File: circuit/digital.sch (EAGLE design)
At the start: 34 parts, among them IC1 MCP1701-5V, IC2 MCP1700-3.3V, X1 MINI-USB-SCHIELD-32005-301

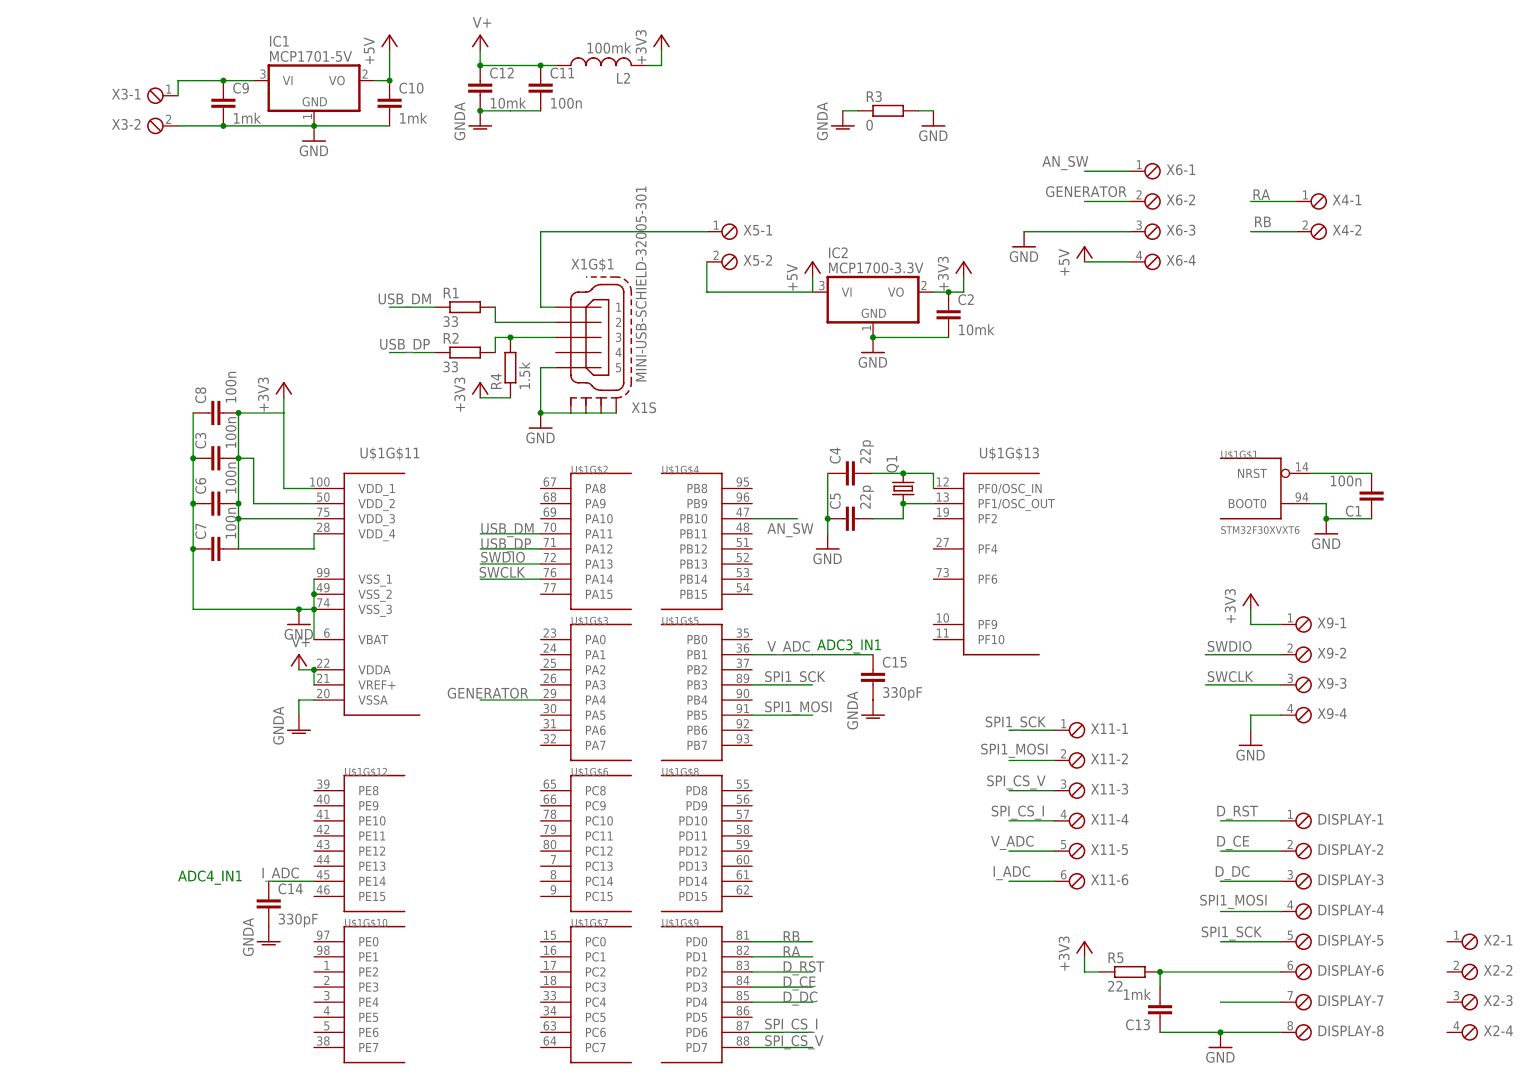
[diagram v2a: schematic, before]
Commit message: - прикрутили коннектор для энкодера
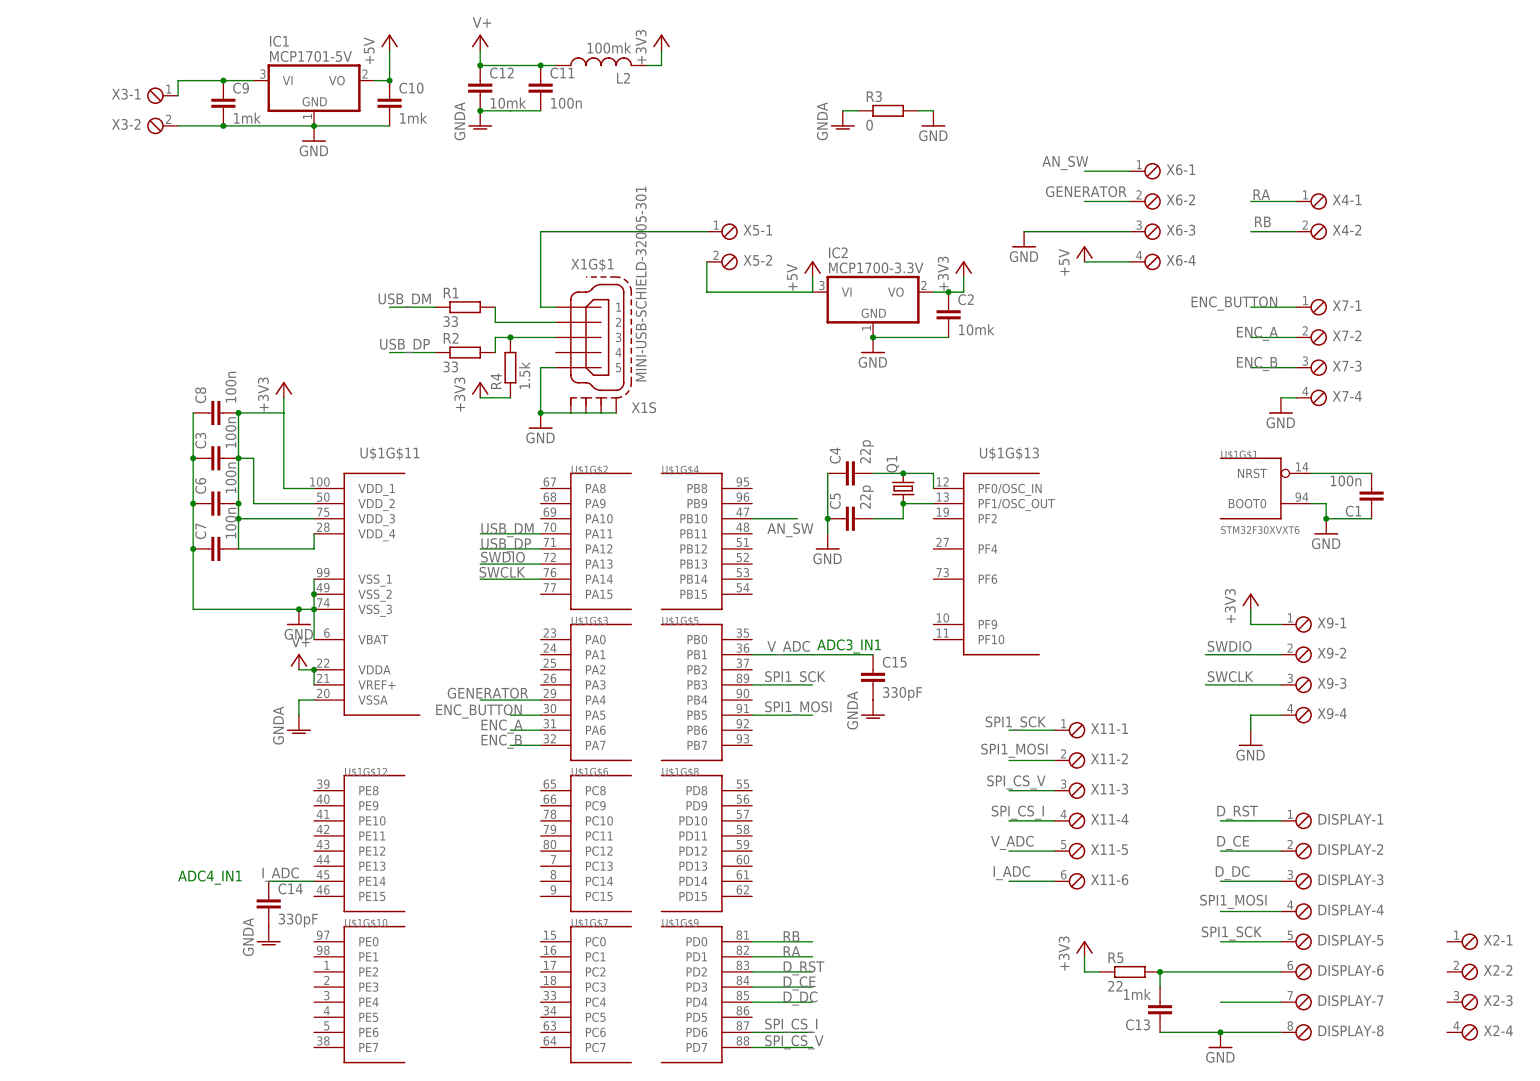
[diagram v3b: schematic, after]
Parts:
- added X7: (no value), con-phoenix-254:MPT4
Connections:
- new net ENC_A: U$1G$3.PA6, X7-2.1
- new net ENC_B: U$1G$3.PA7, X7-3.1
- new net ENC_BUTTON: U$1G$3.PA5, X7-1.1
- net GND: now also X7-4.1
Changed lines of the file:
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@@
 <part name="GND16" library="supply1" deviceset="GND" device=""/>
 <part name="X2" library="con-phoenix-254" deviceset="MPT4" device=""/>
+<part name="X7" library="con-phoenix-254" deviceset="MPT4" device=""/>
+<part name="GND2" library="supply1" deviceset="GND" device=""/>
 </parts>
 <sheets>
@@
 <instance part="X2" gate="-3" x="205.74" y="-58.42"/>
 <instance part="X2" gate="-4" x="205.74" y="-63.5"/>
+<instance part="X7" gate="-1" x="180.34" y="58.42"/>
+<instance part="X7" gate="-2" x="180.34" y="53.34"/>
+<instance part="X7" gate="-3" x="180.34" y="48.26"/>
+<instance part="X7" gate="-4" x="180.34" y="43.18"/>
+<instance part="GND2" gate="1" x="175.26" y="40.64"/>
 </instances>
 <busses>
@@
 <pinref part="GND16" gate="1" pin="GND"/>
 <wire x1="132.08" y1="71.12" x2="142.24" y2="71.12" width="0.1524" layer="91"/>
+</segment>
+<segment>
+<pinref part="X7" gate="-4" pin="1"/>
+<wire x1="177.8" y1="43.18" x2="175.26" y2="43.18" width="0.1524" layer="91"/>
+<pinref part="GND2" gate="1" pin="GND"/>
 </segment>
 </net>
@@
 </segment>
 </net>
+<net name="ENC_BUTTON" class="0">
+<segment>
+<pinref part="X7" gate="-1" pin="1"/>
+<wire x1="177.8" y1="58.42" x2="170.18" y2="58.42" width="0.1524" layer="91"/>
+<label x="160.02" y="58.42" size="1.778" layer="95"/>
+</segment>
+<segment>
+<pinref part="U$1" gate="G$3" pin="PA5"/>
+<wire x1="50.8" y1="-10.16" x2="45.72" y2="-10.16" width="0.1524" layer="91"/>
+<label x="33.02" y="-10.16" size="1.778" layer="95"/>
+</segment>
+</net>
+<net name="ENC_A" class="0">
+<segment>
+<pinref part="X7" gate="-2" pin="1"/>
+<wire x1="177.8" y1="53.34" x2="170.18" y2="53.34" width="0.1524" layer="91"/>
+<label x="167.64" y="53.34" size="1.778" layer="95"/>
+</segment>
+<segment>
+<pinref part="U$1" gate="G$3" pin="PA6"/>
+<wire x1="50.8" y1="-12.7" x2="45.72" y2="-12.7" width="0.1524" layer="91"/>
+<label x="40.64" y="-12.7" size="1.778" layer="95"/>
+</segment>
+</net>
+<net name="ENC_B" class="0">
+<segment>
+<pinref part="X7" gate="-3" pin="1"/>
+<wire x1="177.8" y1="48.26" x2="170.18" y2="48.26" width="0.1524" layer="91"/>
+<label x="167.64" y="48.26" size="1.778" layer="95"/>
+</segment>
+<segment>
+<pinref part="U$1" gate="G$3" pin="PA7"/>
+<wire x1="50.8" y1="-15.24" x2="45.72" y2="-15.24" width="0.1524" layer="91"/>
+<label x="40.64" y="-15.24" size="1.778" layer="95"/>
+</segment>
+</net>

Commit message: - переместили схемы чуть ниже, чтобы уместиться в 49 мм высоты
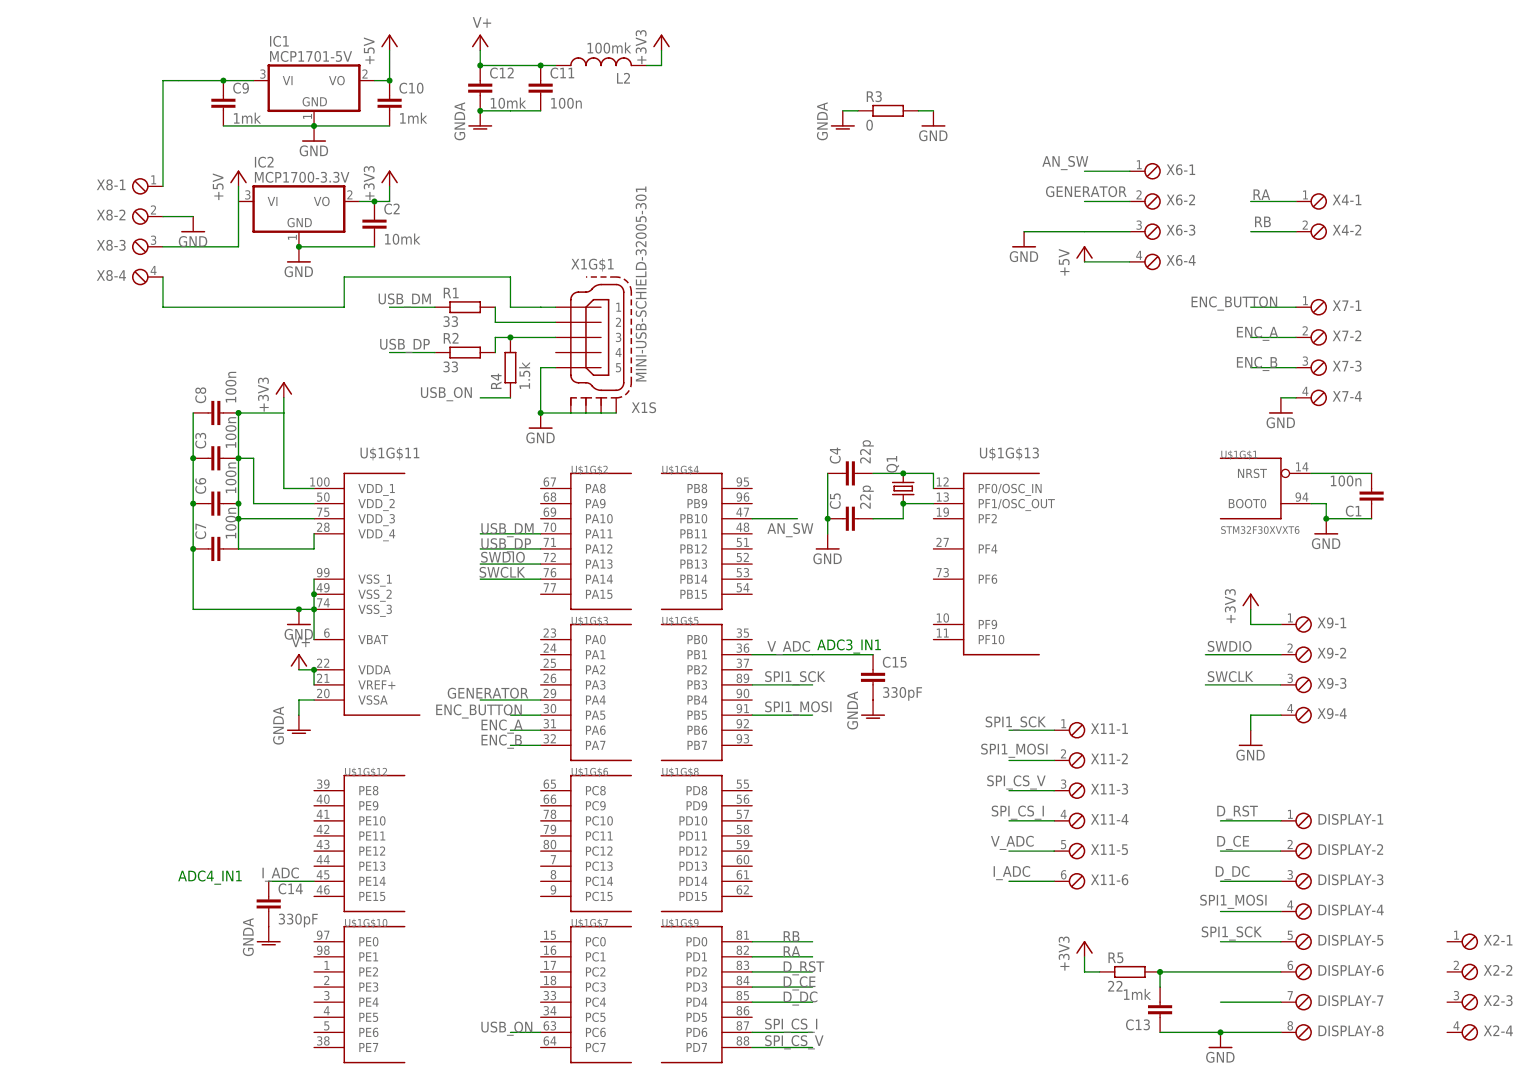
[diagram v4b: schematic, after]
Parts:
- removed X3, X5: (no value), con-phoenix-254:MPT2
- added X8: (no value), con-phoenix-254:MPT4
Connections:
- new net USB_ON: R4.1, U$1G$7.PC6
- net +3V3: no longer R4.1
- net +5V: now also X8-3.1; no longer X5-2.1
- net GND: now also X8-2.1; no longer X3-2.1
- net N$7: now also X8-1.1; no longer X3-1.1
- net N$8: now also X8-4.1; no longer X5-1.1
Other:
- moved on the sheet: C2, IC2
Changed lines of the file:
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@@
 <part name="C8" library="rcl" deviceset="C-EU" device="C0603" value="100n"/>
 <part name="+3V3" library="supply1" deviceset="+3V3" device=""/>
-<part name="X3" library="con-phoenix-254" deviceset="MPT2" device=""/>
 <part name="GND8" library="supply1" deviceset="GND" device=""/>
 <part name="GND9" library="supply1" deviceset="GNDA" device=""/>
@@
 <part name="GND12" library="supply1" deviceset="GND" device=""/>
 <part name="R4" library="rcl" deviceset="R-EU_" device="R0603" value="1.5k"/>
-<part name="+3V5" library="supply1" deviceset="+3V3" device=""/>
 <part name="X11" library="con-phoenix-254" deviceset="MPT6" device=""/>
 <part name="DISPLAY" library="con-phoenix-254" deviceset="MPT8" device=""/>
@@
 <part name="C13" library="rcl" deviceset="C-EU" device="C0603" value="1mk"/>
 <part name="R5" library="rcl" deviceset="R-EU_" device="R0603" value="22"/>
-<part name="X5" library="con-phoenix-254" deviceset="MPT2" device=""/>
 <part name="C14" library="rcl" deviceset="C-EU" device="C0805" value="330pF"/>
 <part name="GND14" library="supply1" deviceset="GNDA" device=""/>
@@
 <part name="X7" library="con-phoenix-254" deviceset="MPT4" device=""/>
 <part name="GND2" library="supply1" deviceset="GND" device=""/>
+<part name="X8" library="con-phoenix-254" deviceset="MPT4" device=""/>
+<part name="GND17" library="supply1" deviceset="GND" device=""/>
 </parts>
 <sheets>
@@
 <instance part="SUPPLY1" gate="1" x="40.64" y="104.14"/>
 <instance part="IC1" gate="G$1" x="12.7" y="96.52"/>
-<instance part="IC2" gate="G$1" x="106.68" y="60.96"/>
+<instance part="IC2" gate="G$1" x="10.16" y="76.2"/>
 <instance part="X1" gate="G$1" x="58.42" y="53.34"/>
 <instance part="X1" gate="S" x="58.42" y="43.18"/>
-<instance part="P+1" gate="1" x="96.52" y="66.04"/>
+<instance part="P+1" gate="1" x="0" y="81.28"/>
 <instance part="R1" gate="G$1" x="38.1" y="58.42"/>
 <instance part="R2" gate="G$1" x="38.1" y="50.8"/>
@@
 <instance part="GND1" gate="1" x="182.88" y="20.32"/>
 <instance part="GND3" gate="1" x="50.8" y="38.1"/>
-<instance part="GND4" gate="1" x="106.68" y="50.8"/>
-<instance part="C2" gate="G$1" x="119.38" y="58.42"/>
+<instance part="GND4" gate="1" x="10.16" y="66.04"/>
+<instance part="C2" gate="G$1" x="22.86" y="73.66"/>
 <instance part="C3" gate="G$1" x="-5.08" y="33.02" rot="R90"/>
-<instance part="+3V1" gate="G$1" x="121.92" y="66.04"/>
+<instance part="+3V1" gate="G$1" x="25.4" y="81.28"/>
 <instance part="+3V2" gate="G$1" x="71.12" y="104.14"/>
 <instance part="Q1" gate="G$1" x="111.76" y="27.94" rot="R90"/>
@@
 <instance part="C8" gate="G$1" x="-5.08" y="40.64" rot="R90"/>
 <instance part="+3V3" gate="G$1" x="7.62" y="45.72"/>
-<instance part="X3" gate="-1" x="-12.7" y="93.98" rot="MR0"/>
-<instance part="X3" gate="-2" x="-12.7" y="88.9" rot="MR0"/>
 <instance part="GND8" gate="1" x="116.84" y="88.9"/>
 <instance part="GND9" gate="1" x="101.6" y="88.9"/>
@@
 <instance part="GND12" gate="1" x="170.18" y="-15.24"/>
 <instance part="R4" gate="G$1" x="45.72" y="48.26" rot="R90"/>
-<instance part="+3V5" gate="G$1" x="40.64" y="45.72"/>
 <instance part="X11" gate="-1" x="139.7" y="-12.7"/>
 <instance part="X11" gate="-2" x="139.7" y="-17.78"/>
@@
 <instance part="C13" gate="G$1" x="154.94" y="-60.96" rot="R180"/>
 <instance part="R5" gate="G$1" x="149.86" y="-53.34"/>
-<instance part="X5" gate="-1" x="81.28" y="71.12"/>
-<instance part="X5" gate="-2" x="81.28" y="66.04"/>
 <instance part="C14" gate="G$1" x="5.08" y="-40.64"/>
 <instance part="GND14" gate="1" x="5.08" y="-48.26"/>
@@
 <instance part="X7" gate="-4" x="180.34" y="43.18"/>
 <instance part="GND2" gate="1" x="175.26" y="40.64"/>
+<instance part="X8" gate="-1" x="-15.24" y="78.74" rot="MR0"/>
+<instance part="X8" gate="-2" x="-15.24" y="73.66" rot="MR0"/>
+<instance part="X8" gate="-3" x="-15.24" y="68.58" rot="MR0"/>
+<instance part="X8" gate="-4" x="-15.24" y="63.5" rot="MR0"/>
+<instance part="GND17" gate="1" x="-7.62" y="71.12"/>
 </instances>
 <busses>
@@
 <pinref part="P+1" gate="1" pin="+5V"/>
 <pinref part="IC2" gate="G$1" pin="VI"/>
-<wire x1="96.52" y1="63.5" x2="96.52" y2="60.96" width="0.1524" layer="91"/>
-<pinref part="X5" gate="-2" pin="1"/>
-<wire x1="96.52" y1="60.96" x2="78.74" y2="60.96" width="0.1524" layer="91"/>
-<wire x1="78.74" y1="60.96" x2="78.74" y2="66.04" width="0.1524" layer="91"/>
+<wire x1="0" y1="78.74" x2="0" y2="76.2" width="0.1524" layer="91"/>
+<wire x1="0" y1="76.2" x2="0" y2="68.58" width="0.1524" layer="91"/>
+<pinref part="X8" gate="-3" pin="1"/>
+<wire x1="0" y1="68.58" x2="-12.7" y2="68.58" width="0.1524" layer="91"/>
 </segment>
 <segment>
@@
 <pinref part="GND4" gate="1" pin="GND"/>
 <pinref part="C2" gate="G$1" pin="2"/>
-<wire x1="106.68" y1="53.34" x2="119.38" y2="53.34" width="0.1524" layer="91"/>
-<junction x="106.68" y="53.34"/>
+<wire x1="10.16" y1="68.58" x2="22.86" y2="68.58" width="0.1524" layer="91"/>
+<junction x="10.16" y="68.58"/>
 </segment>
 <segment>
@@
 <wire x1="-2.54" y1="88.9" x2="12.7" y2="88.9" width="0.1524" layer="91"/>
 <pinref part="C10" gate="G$1" pin="2"/>
-<pinref part="X3" gate="-2" pin="1"/>
-<wire x1="-10.16" y1="88.9" x2="-2.54" y2="88.9" width="0.1524" layer="91"/>
 <junction x="12.7" y="88.9"/>
-<junction x="-2.54" y="88.9"/>
 </segment>
 <segment>
@@
 <pinref part="GND2" gate="1" pin="GND"/>
 </segment>
+<segment>
+<pinref part="GND17" gate="1" pin="GND"/>
+<pinref part="X8" gate="-2" pin="1"/>
+<wire x1="-7.62" y1="73.66" x2="-12.7" y2="73.66" width="0.1524" layer="91"/>
+</segment>
 </net>
 <net name="N$3" class="0">
@@
 <segment>
 <pinref part="+3V1" gate="G$1" pin="+3V3"/>
-<wire x1="121.92" y1="63.5" x2="121.92" y2="60.96" width="0.1524" layer="91"/>
+<wire x1="25.4" y1="78.74" x2="25.4" y2="76.2" width="0.1524" layer="91"/>
 <pinref part="C2" gate="G$1" pin="1"/>
 <pinref part="IC2" gate="G$1" pin="VO"/>
-<wire x1="116.84" y1="60.96" x2="119.38" y2="60.96" width="0.1524" layer="91"/>
-<wire x1="121.92" y1="60.96" x2="119.38" y2="60.96" width="0.1524" layer="91"/>
-<junction x="119.38" y="60.96"/>
+<wire x1="20.32" y1="76.2" x2="22.86" y2="76.2" width="0.1524" layer="91"/>
+<wire x1="25.4" y1="76.2" x2="22.86" y2="76.2" width="0.1524" layer="91"/>
+<junction x="22.86" y="76.2"/>
 </segment>
 <segment>
@@
 </segment>
 <segment>
-<pinref part="R4" gate="G$1" pin="1"/>
-<pinref part="+3V5" gate="G$1" pin="+3V3"/>
-<wire x1="45.72" y1="43.18" x2="40.64" y2="43.18" width="0.1524" layer="91"/>
-</segment>
-<segment>
 <pinref part="R5" gate="G$1" pin="1"/>
 <pinref part="+3V6" gate="G$1" pin="+3V3"/>
@@
 <pinref part="IC1" gate="G$1" pin="VI"/>
 <wire x1="-2.54" y1="96.52" x2="2.54" y2="96.52" width="0.1524" layer="91"/>
-<pinref part="X3" gate="-1" pin="1"/>
-<wire x1="-10.16" y1="93.98" x2="-10.16" y2="96.52" width="0.1524" layer="91"/>
 <wire x1="-10.16" y1="96.52" x2="-2.54" y2="96.52" width="0.1524" layer="91"/>
 <junction x="-2.54" y="96.52"/>
+<pinref part="X8" gate="-1" pin="1"/>
+<wire x1="-10.16" y1="96.52" x2="-12.7" y2="96.52" width="0.1524" layer="91"/>
+<wire x1="-12.7" y1="96.52" x2="-12.7" y2="78.74" width="0.1524" layer="91"/>
 </segment>
 </net>
@@
 <pinref part="X1" gate="G$1" pin="1"/>
 <wire x1="53.34" y1="58.42" x2="50.8" y2="58.42" width="0.1524" layer="91"/>
-<wire x1="50.8" y1="58.42" x2="50.8" y2="71.12" width="0.1524" layer="91"/>
-<pinref part="X5" gate="-1" pin="1"/>
-<wire x1="50.8" y1="71.12" x2="78.74" y2="71.12" width="0.1524" layer="91"/>
+<wire x1="50.8" y1="58.42" x2="45.72" y2="58.42" width="0.1524" layer="91"/>
+<wire x1="45.72" y1="58.42" x2="45.72" y2="63.5" width="0.1524" layer="91"/>
+<wire x1="45.72" y1="63.5" x2="17.78" y2="63.5" width="0.1524" layer="91"/>
+<wire x1="17.78" y1="63.5" x2="17.78" y2="58.42" width="0.1524" layer="91"/>
+<pinref part="X8" gate="-4" pin="1"/>
+<wire x1="17.78" y1="58.42" x2="-12.7" y2="58.42" width="0.1524" layer="91"/>
+<wire x1="-12.7" y1="58.42" x2="-12.7" y2="63.5" width="0.1524" layer="91"/>
 </segment>
 </net>
@@
 </segment>
 </net>
+<net name="USB_ON" class="0">
+<segment>
+<pinref part="U$1" gate="G$7" pin="PC6"/>
+<wire x1="50.8" y1="-63.5" x2="45.72" y2="-63.5" width="0.1524" layer="91"/>
+<label x="40.64" y="-63.5" size="1.778" layer="95"/>
+</segment>
+<segment>
+<pinref part="R4" gate="G$1" pin="1"/>
+<wire x1="45.72" y1="43.18" x2="40.64" y2="43.18" width="0.1524" layer="91"/>
+<label x="30.48" y="43.18" size="1.778" layer="95"/>
+</segment>
+</net>
